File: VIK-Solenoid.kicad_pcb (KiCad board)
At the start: 2 copper layers, 25 x 42 mm, 11 parts, among them J1 Conn_01x02_Female, J2 vik-module-connector, J3 Conn_01x03_Pin, Q1 TIP120

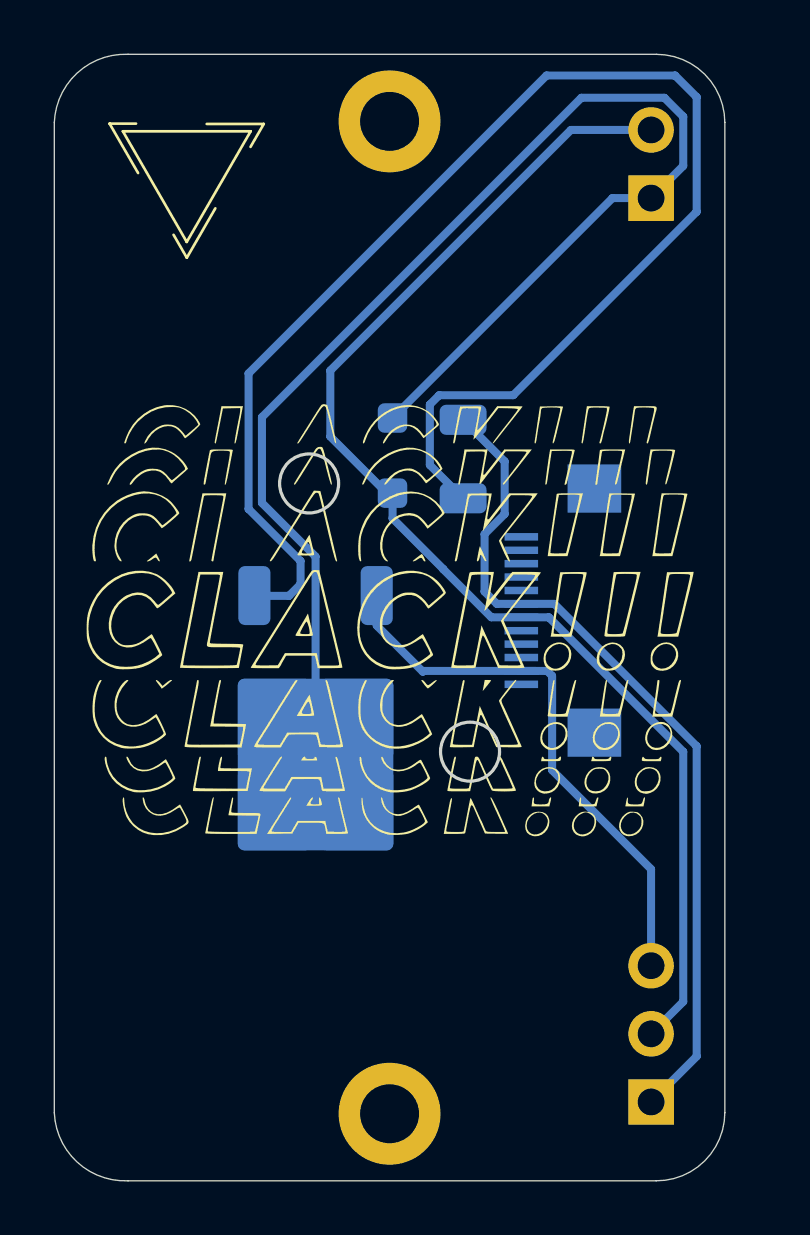
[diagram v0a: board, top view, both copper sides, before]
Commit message: XS version
Extra Small Variant
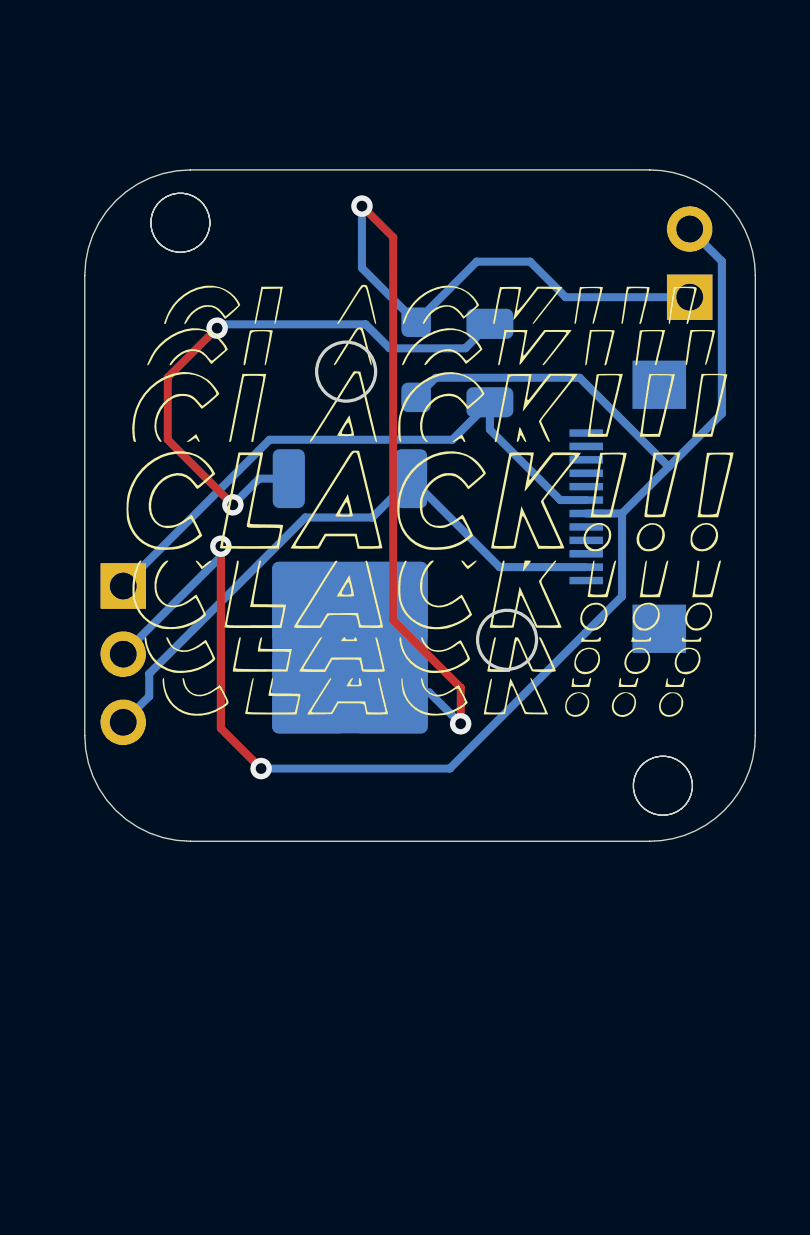
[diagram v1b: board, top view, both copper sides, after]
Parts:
- removed the REF** at (192.1, 87.4)
- removed the REF** at (184.5, 70.8)
- added ?: , , F.Cu at (202.2, 93.7)
- added ?: , , F.Cu at (184.2, 72.7)
- added REF**: MountingHole_2.2mm_M2_ISO7380, MountingHole:MountingHole_2.2mm_M2_ISO7380, F.Cu at (202.2, 93.7)
- added REF**: MountingHole_2.2mm_M2_ISO7380, MountingHole:MountingHole_2.2mm_M2_ISO7380, F.Cu at (184.2, 72.7)
- moved J3 27.5 mm to (182.1, 86.2), turned to 0 degrees
- moved REF** 7.28 mm to (184.7, 78.0)
- moved G*** 4.69 mm to (193.5, 83.0)
- moved J2 4.56 mm to (201.4, 83.3)
- moved Q1 4.54 mm to (190.6, 87.2)
- moved REF** 4.39 mm to (193.4, 83.2)
- moved J1 3.97 mm to (203.2, 75.4)
- moved R1 3.72 mm to (195.8, 77.9), turned to -90 degrees
- moved D1 3.68 mm to (193.0, 77.8)
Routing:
- net Net-(Q1-B): track 53.7 -> 21.8 mm, vias 0 -> 2
- net +5V: track 47.7 -> 58.7 mm, vias 0 -> 2
- net Net-(D1-A): track 51.5 -> 40.8 mm, vias 0 -> 2
- net Solenoid: track 31.6 -> 22.2 mm
- net GND: track 21.3 -> 22.9 mm
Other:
- board size 25 x 42 mm -> 25 x 25 mm
- board text added: "IO"
- board text removed: "GPIO"
